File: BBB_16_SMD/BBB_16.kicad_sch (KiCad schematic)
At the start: 45 parts, among them J17 Power In Left, J18 Power In Right, J19 GPIO, J23 VIN Voltage, J24 Expansion Header, J25 RTC Conn, J26 OLED, J27 Aux Pwr, J28 VIN Select, Q1 DMP3056L, SW1 Left BTN, SW2 Up BTN, SW3 Down BTN, SW4 Right BTN, SW5 PWR BTN, U2 Universe5V, U6 24L256

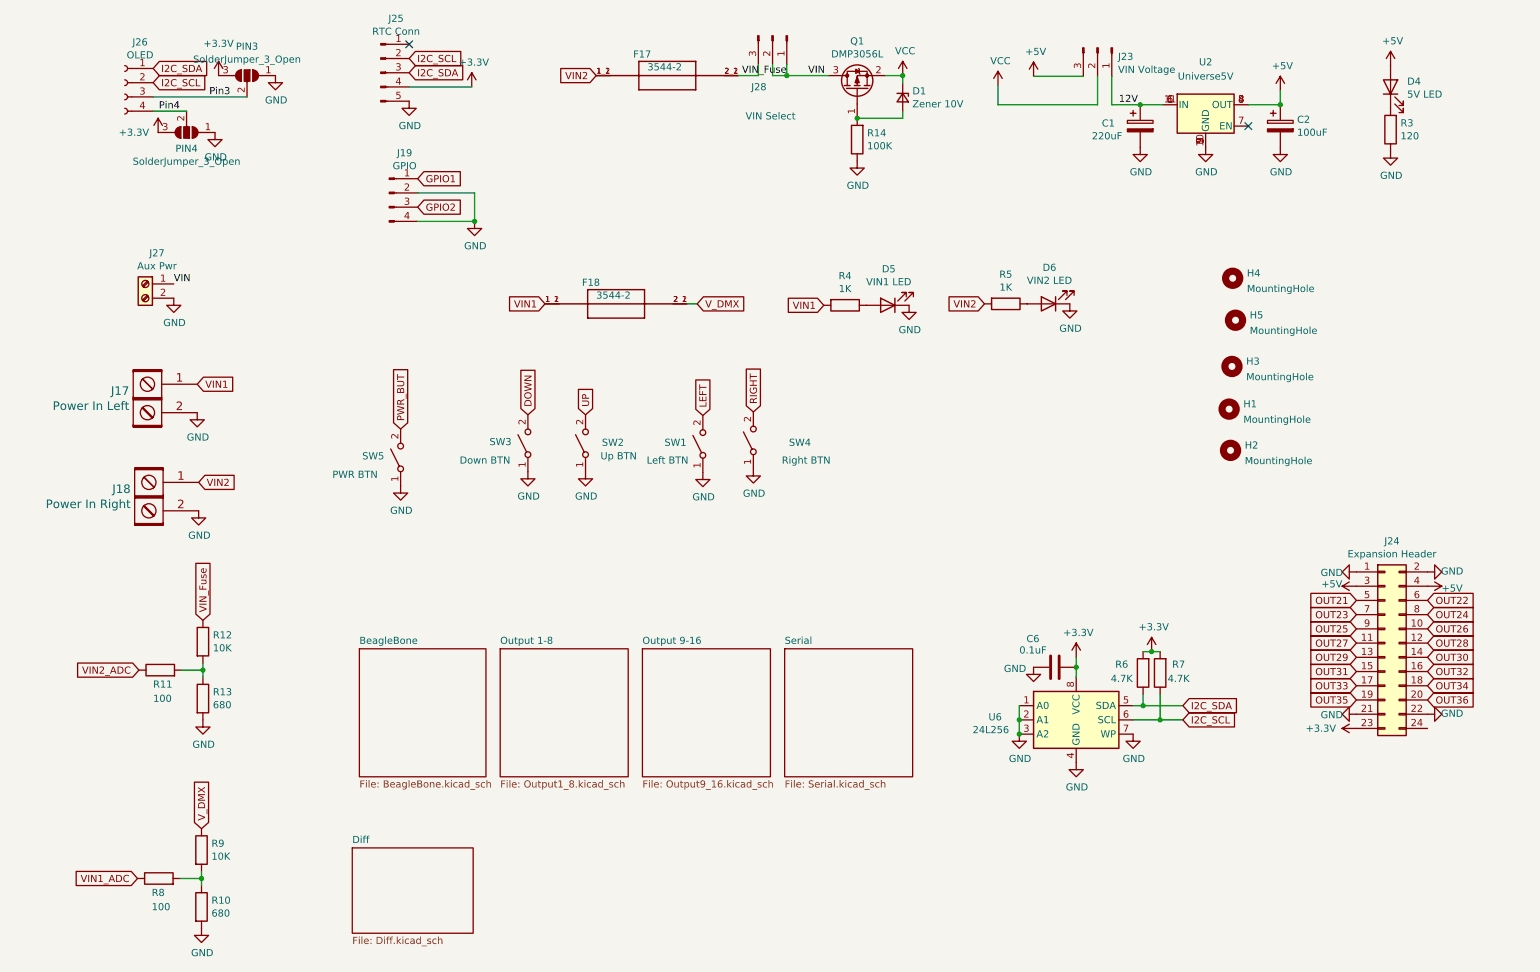
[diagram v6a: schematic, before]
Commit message: added wings
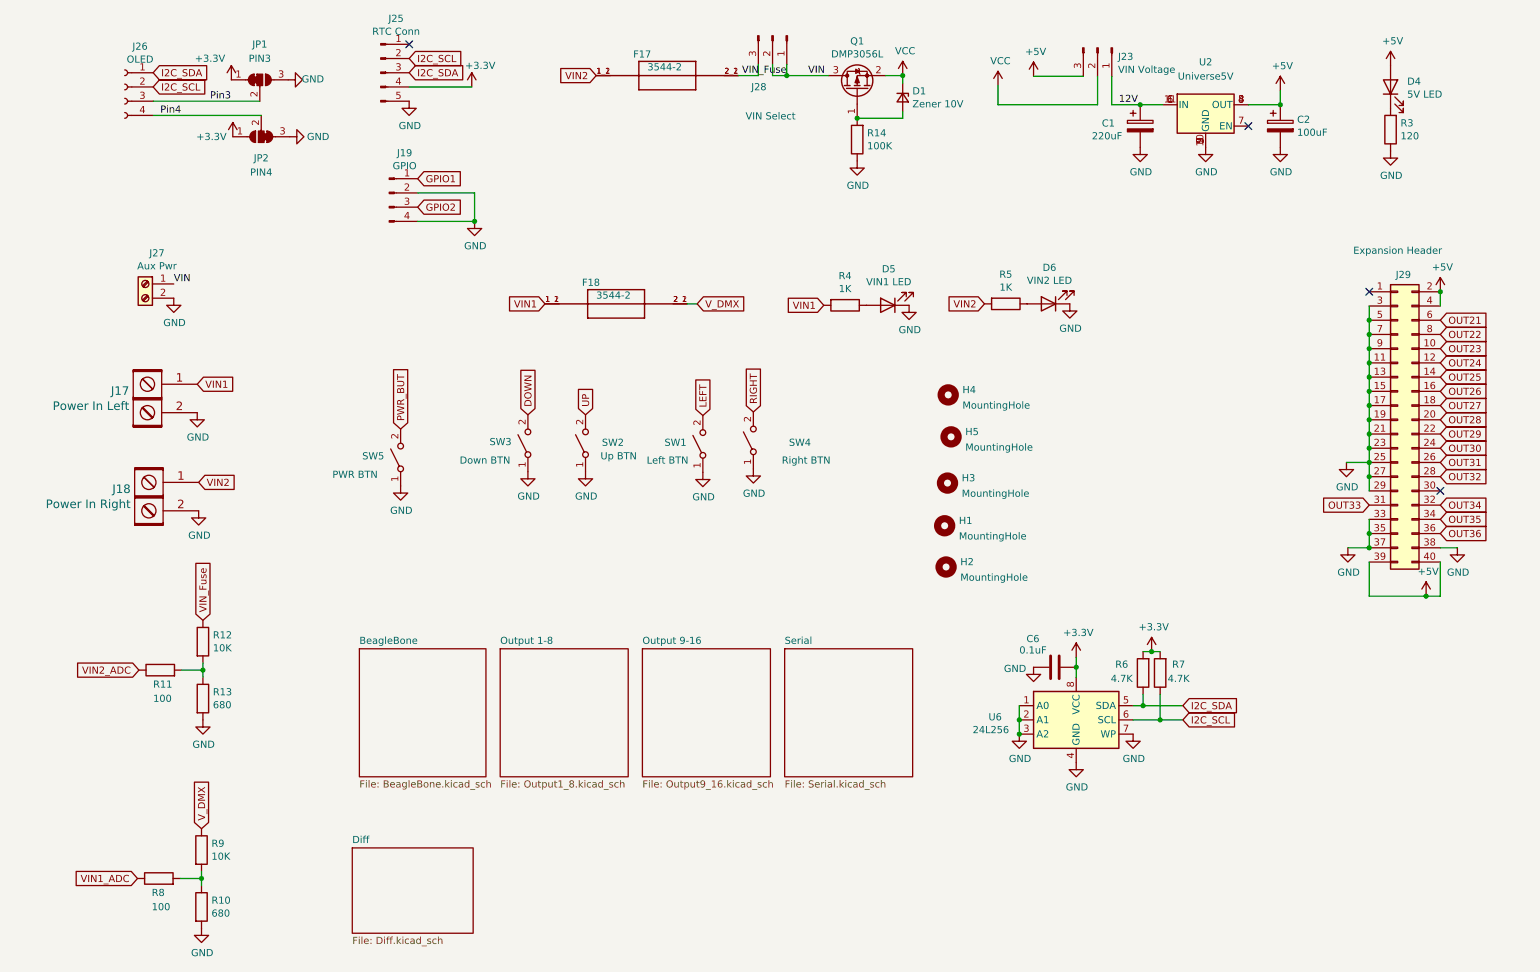
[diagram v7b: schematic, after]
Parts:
- removed J24: Expansion Header, 302-S241:OST_302-S241, symbol Connector_Generic:Conn_02x12_Odd_Even
- removed PIN3, PIN4: SolderJumper_3_Open, Jumper:SolderJumper-3_P1.3mm_Open_Pad1.0x1.5mm, symbol Jumper:SolderJumper_3_Open
- added J29: Expansion Header, Connector_IDC:IDC-Header_2x20_P2.54mm_Vertical, symbol Connector_Generic:Conn_02x20_Odd_Even
- added JP1: PIN3, Scotts:SolderJumper-3_P1mm_Bridged12, symbol Jumper:SolderJumper_3_Bridged12
- added JP2: PIN4, Scotts:SolderJumper-3_P1mm_Bridged23, symbol Scotts:SolderJumper_3_Bridged23
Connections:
- net +3V3: now also JP1.1 (A), JP2.1 (A)
- net +5V: now also J29.2 (Pin_2), J29.39 (Pin_39), J29.4 (Pin_4), J29.40 (Pin_40)
- net GND: now also J29.11 (Pin_11), J29.13 (Pin_13), J29.15 (Pin_15), J29.17 (Pin_17), J29.19 (Pin_19), J29.21 (Pin_21), J29.23 (Pin_23), J29.25 (Pin_25), J29.27 (Pin_27), J29.29 (Pin_29), J29.3 (Pin_3), J29.33 (Pin_33), J29.35 (Pin_35), J29.37 (Pin_37), J29.38 (Pin_38), J29.5 (Pin_5), J29.7 (Pin_7), J29.9 (Pin_9), JP1.3 (B), JP2.3 (B)
- net OUT21: now also J29.6 (Pin_6)
- net OUT22: now also J29.8 (Pin_8)
- net OUT23: now also J29.10 (Pin_10)
- net OUT24: now also J29.12 (Pin_12)
- net OUT25: now also J29.14 (Pin_14)
- net OUT26: now also J29.16 (Pin_16)
- net OUT27: now also J29.18 (Pin_18)
- net OUT28: now also J29.20 (Pin_20)
- net OUT29: now also J29.22 (Pin_22)
- net OUT30: now also J29.24 (Pin_24)
- net OUT31: now also J29.26 (Pin_26)
- net OUT32: now also J29.28 (Pin_28)
- net OUT33: now also J29.31 (Pin_31)
- net OUT34: now also J29.32 (Pin_32)
- net OUT35: now also J29.34 (Pin_34)
- net OUT36: now also J29.36 (Pin_36)
- net Pin3: now also JP1.2 (C)
- net Pin4: now also JP2.2 (C)
- no-connect marks 2 -> 4
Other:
- moved on the sheet: H1, H2, H3, H4, H5, J26
